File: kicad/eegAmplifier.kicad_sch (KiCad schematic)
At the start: 26 parts, among them U1 TLC274, U2 TL074, U5 AD620

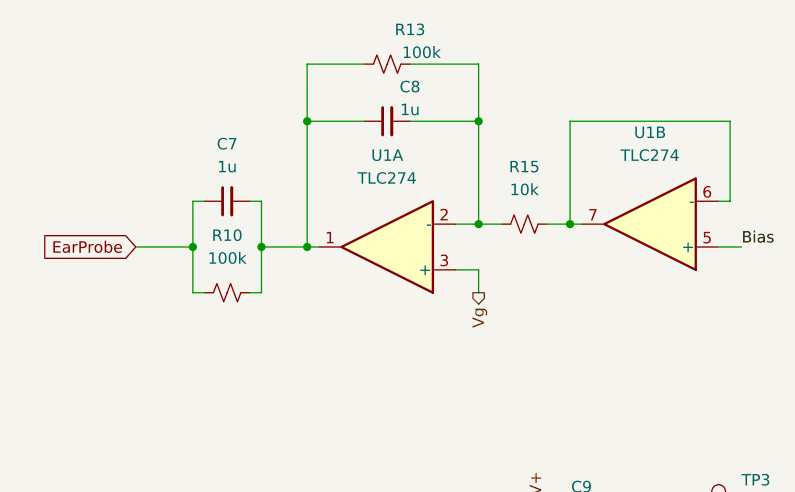
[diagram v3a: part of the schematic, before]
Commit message: Change buzzer pin, i2c pins, ADC plugin, ground pin.
- Change buzzer PWM pin for easier routing.
- Use i2c1 on P2_9(SCL) and P2_11(SDA)
- Use ADS1115 breakout board via header
- Add ground pin next to test points.
- Add header for battery.
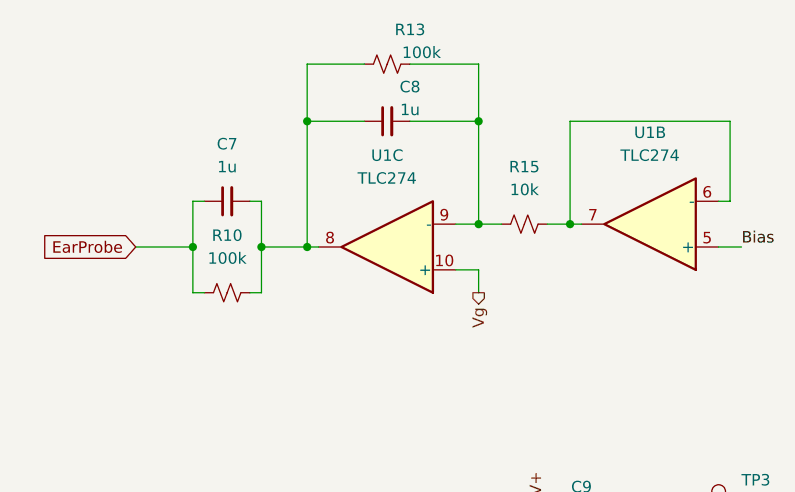
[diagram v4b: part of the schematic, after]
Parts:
- removed unit 1 of U1
- added unit 3 of U1
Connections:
- net Vg: now also U1.10 (+)
- net at C7.2, C8.1, R10.2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: now also U1.8
- net at C8.2, R13.2, R15.1: now also U1.9 (-)
- net GNDS renamed GND
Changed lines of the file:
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@@
     (pin "2")
-  )
-  (symbol (lib_id "Amplifier_Operational:TLC274") (at 102.87 76.2 180) (unit 1)
-    (in_bom yes) (on_board yes) (fields_autoplaced)
-    (property "Reference" "U1" (id 0) (at 102.87 66.04 0))
-    (property "Value" "TLC274" (id 1) (at 102.87 68.58 0))
-    (property "Footprint" "Package_DIP:DIP-14_W7.62mm_LongPads" (id 2) (at 104.14 78.74 0)
-      (effects (font (size 1.27 1.27)) hide)
-    )
-    (property "Datasheet" "http://www.ti.com/lit/ds/symlink/tlc274.pdf" (id 3) (at 101.6 81.28 0)
-      (effects (font (size 1.27 1.27)) hide)
-    )
-    (pin "1")
-    (pin "2")
-    (pin "3")
   )
   (symbol (lib_id "Device:R_Small_US") (at 102.87 55.88 90) (unit 1)
@@
     (pin "8")
   )
+  (symbol (lib_id "Amplifier_Operational:TLC274") (at 102.87 76.2 180) (unit 3)
+    (in_bom yes) (on_board yes) (fields_autoplaced)
+    (property "Reference" "U1" (id 0) (at 102.87 66.04 0))
+    (property "Value" "TLC274" (id 1) (at 102.87 68.58 0))
+    (property "Footprint" "Package_DIP:DIP-14_W7.62mm_LongPads" (id 2) (at 104.14 78.74 0)
+      (effects (font (size 1.27 1.27)) hide)
+    )
+    (property "Datasheet" "http://www.ti.com/lit/ds/symlink/tlc274.pdf" (id 3) (at 101.6 81.28 0)
+      (effects (font (size 1.27 1.27)) hide)
+    )
+    (pin "10")
+    (pin "8")
+    (pin "9")
+  )
   (symbol (lib_id "Device:R_Small_US") (at 201.93 143.51 0) (unit 1)
     (in_bom yes) (on_board yes) (fields_autoplaced)
@@
     (pin "3")
   )
-  (symbol (lib_id "power:GNDS") (at 128.27 111.76 0) (unit 1)
+  (symbol (lib_id "power:GND") (at 128.27 111.76 0) (unit 1)
     (in_bom yes) (on_board yes)
     (property "Reference" "#PWR025" (id 0) (at 128.27 118.11 0)
@@
     (pin "2")
   )
-  (symbol (lib_id "power:GNDS") (at 166.37 146.05 0) (unit 1)
+  (symbol (lib_id "power:GND") (at 166.37 146.05 0) (unit 1)
     (in_bom yes) (on_board yes) (fields_autoplaced)
     (property "Reference" "#PWR026" (id 0) (at 166.37 152.4 0)
